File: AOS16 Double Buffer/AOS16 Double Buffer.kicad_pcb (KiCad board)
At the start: 4 copper layers, 100 x 100 mm, 18 parts, among them IC1 SN74AUP2G14DCKR, IC10 SN74LVC16245ADGVR, IC11 SN74LVC16245ADGVR, IC2 SN74LVC16245ADGVR, IC3 IS61WV3216BLL-12TLI, IC4 SN74LVC16245ADGVR, IC5 SN74LVC16245ADGVR, IC6 SN74LVC16245ADGVR, IC7 IS61WV3216BLL-12TLI, IC8 SN74LVC16245ADGVR, IC9 SN74LVC16245ADGVR, J1 Conn_01x07_Pin, J2 Conn_02x08_Top_Bottom, J3 Conn_02x08_Odd_Even, J4 Conn_02x08_Odd_Even, J5 Conn_02x08_Top_Bottom, U1 74LS157, U2 74LS157

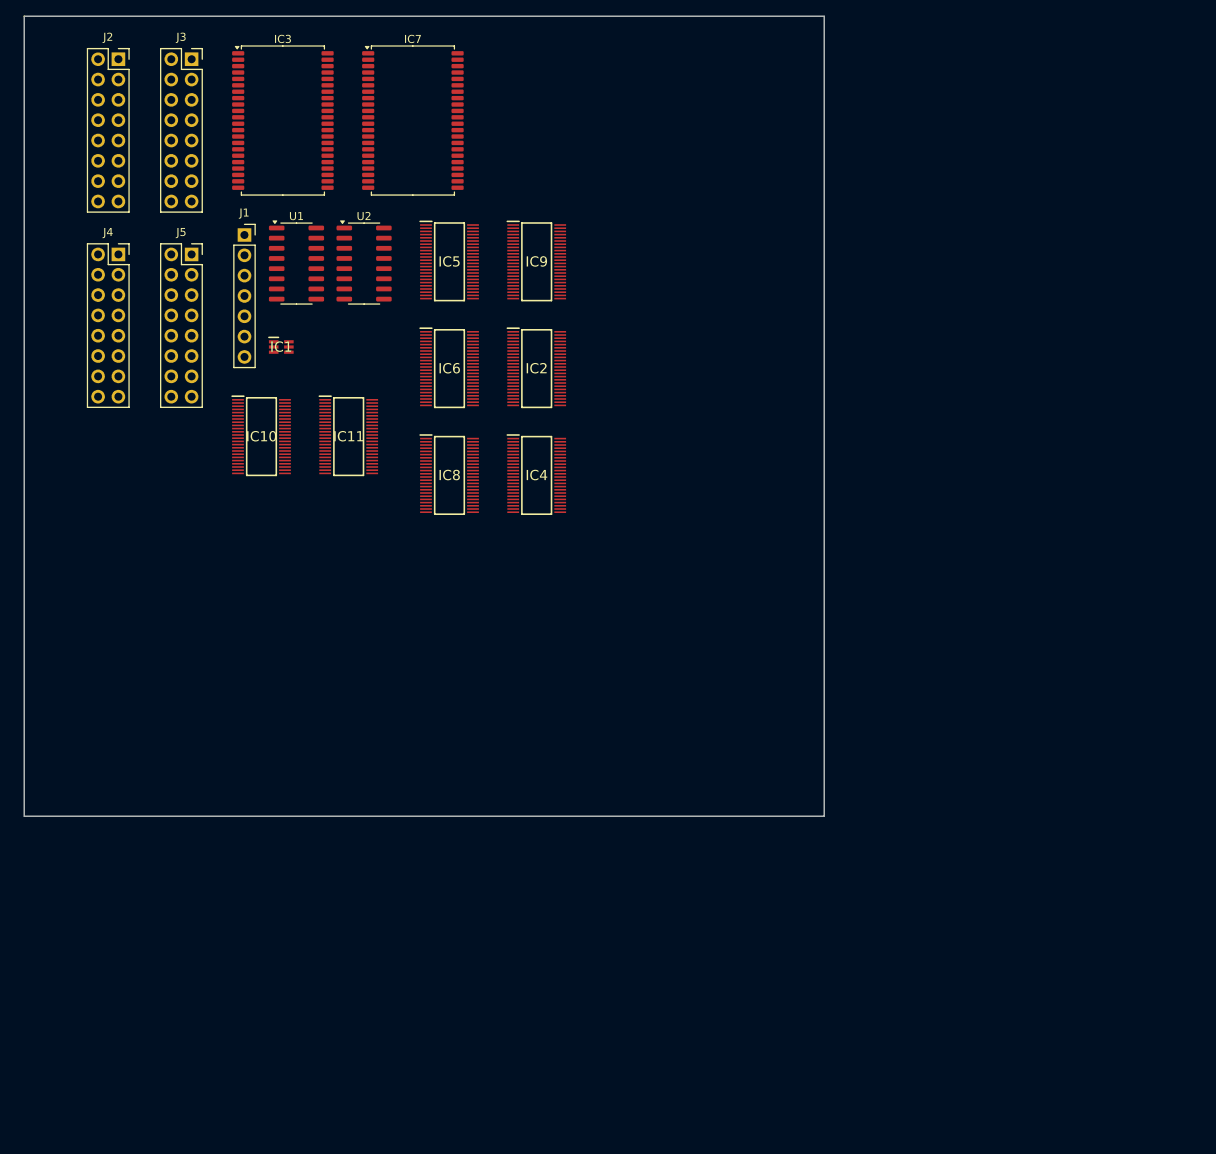
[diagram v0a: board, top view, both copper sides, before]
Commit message: updated double buffer
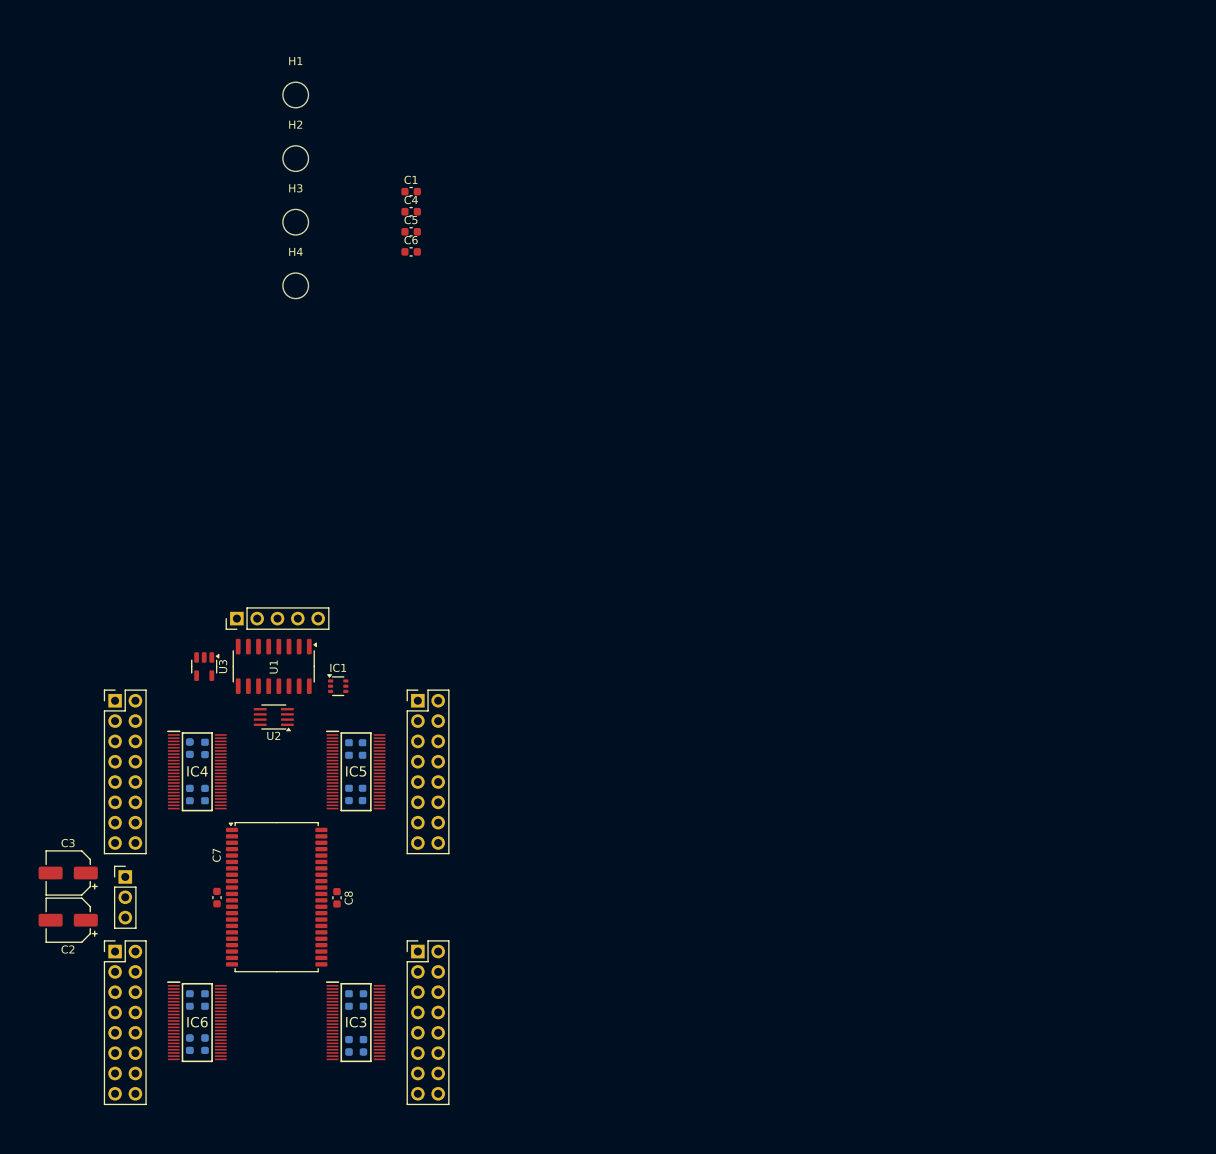
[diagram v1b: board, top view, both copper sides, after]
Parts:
- removed IC10, IC11, IC8, IC9: SN74LVC16245ADGVR, sn74lvc:SOP40P640X120-48N
- removed IC7: IS61WV3216BLL-12TLI, Package_SO:TSOP-II-44_10.16x18.41mm_P0.8mm
- added C1: 0.1uF, Capacitor_SMD:C_0603_1608Metric, F.Cu at (73.4, 46.9)
- added C10: 0.1uF, Capacitor_SMD:C_0603_1608Metric, B.Cu at (67.3, 116.6)
- added C11: 0.1uF, Capacitor_SMD:C_0603_1608Metric, B.Cu at (67.3, 122.3)
- added C12: 0.1uF, Capacitor_SMD:C_0603_1608Metric, B.Cu at (65.6, 122.3)
- added C13: 0.1uF, Capacitor_SMD:C_0603_1608Metric, B.Cu at (45.7, 116.5)
- added C14: 0.1uF, Capacitor_SMD:C_0603_1608Metric, B.Cu at (47.6, 116.5)
- added C15: 0.1uF, Capacitor_SMD:C_0603_1608Metric, B.Cu at (47.6, 122.3)
- added C16: 0.1uF, Capacitor_SMD:C_0603_1608Metric, B.Cu at (45.7, 122.3)
- added C17: 0.1uF, Capacitor_SMD:C_0603_1608Metric, B.Cu at (65.6, 148.0)
- added C18: 0.1uF, Capacitor_SMD:C_0603_1608Metric, B.Cu at (67.4, 148.0)
- added C19: 0.1uF, Capacitor_SMD:C_0603_1608Metric, B.Cu at (65.6, 153.7)
- added C2: 100 uF, Capacitor_SMD:CP_Elec_5x5.3, F.Cu at (30.5, 138.0)
- added C20: 0.1uF, Capacitor_SMD:C_0603_1608Metric, B.Cu at (67.4, 153.7)
- added C21: 0.1uF, Capacitor_SMD:C_0603_1608Metric, B.Cu at (45.7, 148.0)
- added C22: 0.1uF, Capacitor_SMD:C_0603_1608Metric, B.Cu at (47.6, 148.0)
- added C23: 0.1uF, Capacitor_SMD:C_0603_1608Metric, B.Cu at (47.6, 153.5)
- added C24: 0.1uF, Capacitor_SMD:C_0603_1608Metric, B.Cu at (45.7, 153.5)
- added C3: 100 uF, Capacitor_SMD:CP_Elec_5x5.3, F.Cu at (30.5, 132.1)
- added C4: 0.1uF, Capacitor_SMD:C_0603_1608Metric, F.Cu at (73.4, 49.4)
- added C5: 0.1uF, Capacitor_SMD:C_0603_1608Metric, F.Cu at (73.4, 52.0)
- added C6: 0.1uF, Capacitor_SMD:C_0603_1608Metric, F.Cu at (73.4, 54.5)
- added C7: 0.1uF, Capacitor_SMD:C_0603_1608Metric, F.Cu at (49.1, 135.2)
- added C8: 0.1uF, Capacitor_SMD:C_0603_1608Metric, F.Cu at (64.1, 135.2)
- added C9: 0.1uF, Capacitor_SMD:C_0603_1608Metric, B.Cu at (65.6, 116.6)
- added H1: M3, MountingHole:MountingHole_3.2mm_M3, F.Cu at (58.9, 34.9)
- added H2: M3, MountingHole:MountingHole_3.2mm_M3, F.Cu at (58.9, 42.8)
- added H3: M3, MountingHole:MountingHole_3.2mm_M3, F.Cu at (58.9, 50.8)
- added H4: M3, MountingHole:MountingHole_3.2mm_M3, F.Cu at (58.9, 58.7)
- added J6: Conn_02x08_Top_Bottom, Connector_PinHeader_2.54mm:PinHeader_2x08_P2.54mm_Vertical, F.Cu at (74.2, 110.6)
- added U3: 74AHC1G08, Package_TO_SOT_SMD:SOT-23-5, F.Cu at (47.5, 106.3)
- IC1: footprint sn74aup2:SOT65P210X110-6N -> Package_TO_SOT_SMD:SOT-363_SC-70-6
- IC2: value SN74LVC16245ADGVR -> IS61WV3216BLL-12TLI; footprint sn74lvc:SOP40P640X120-48N -> Package_SO:TSOP-II-44_10.16x18.41mm_P0.8mm
- IC3: value IS61WV3216BLL-12TLI -> SN74LVC16245ADGVR; footprint Package_SO:TSOP-II-44_10.16x18.41mm_P0.8mm -> sn74lvc:SOP40P640X120-48N
- J1: value Conn_01x07_Pin -> Conn_01x03_Pin; footprint Connector_PinSocket_2.54mm:PinSocket_1x07_P2.54mm_Vertical -> Connector_PinHeader_2.54mm:PinHeader_1x03_P2.54mm_Vertical
- J2: value Conn_02x08_Top_Bottom -> Conn_01x05_Pin; footprint Connector_PinSocket_2.54mm:PinSocket_2x08_P2.54mm_Vertical -> Connector_PinHeader_2.54mm:PinHeader_1x05_P2.54mm_Vertical
- J3, J4: value Conn_02x08_Odd_Even -> Conn_02x08_Top_Bottom; footprint Connector_PinSocket_2.54mm:PinSocket_2x08_P2.54mm_Vertical -> Connector_PinHeader_2.54mm:PinHeader_2x08_P2.54mm_Vertical
- J5: footprint Connector_PinSocket_2.54mm:PinSocket_2x08_P2.54mm_Vertical -> Connector_PinHeader_2.54mm:PinHeader_2x08_P2.54mm_Vertical
- U2: value 74LS157 -> 74AUC2G32; footprint Package_SO:SOIC-16_3.9x9.9mm_P1.27mm -> Package_SO:SSOP-8_2.95x2.8mm_P0.65mm
- moved IC3 113.1 mm to (66.5, 150.8)
- moved J3 111.9 mm to (36.4, 141.9)
- moved J4 94.8 mm to (74.2, 141.9)
- moved IC6 87.6 mm to (46.6, 150.8)
- moved J1 81.6 mm to (37.6, 132.6)
- moved IC2 73.6 mm to (56.6, 135.1)
- moved J2 71.5 mm to (51.6, 100.3), turned to 90 degrees
- moved IC5 64.8 mm to (66.5, 119.4)
- moved U2 57.8 mm to (56.2, 112.6), turned to 180 degrees
- moved J5 56.6 mm to (36.4, 110.6)
- moved IC4 56.3 mm to (46.6, 119.4)
- moved U1 50.4 mm to (56.2, 106.3), turned to -90 degrees
- moved IC1 43.0 mm to (64.2, 108.8)
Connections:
- IC1 pad 1: /GSEL -> /SEL
- IC1 pad 3: unconnected-(IC1-2A-Pad3) -> /W1
- IC1 pad 4: unconnected-(IC1-2Y-Pad4) -> /~{W1}
- IC1 pad 6: /~{GSEL} -> /~{SEL}
- IC2 pad 1: VCC -> unconnected-(IC2-NC_1-Pad1)
- IC2 pad 10: GND -> /ram/OUT9
- IC2 pad 11: /word_conn/IN6 -> +3.3V
- IC2 pad 12: /word_conn/IN7 -> GND
- IC2 pad 13: /word_conn/IN8 -> /ram/OUT7
- IC2 pad 14: /word_conn/IN9 -> /ram/OUT5
- IC2 pad 15: GND -> /ram/OUT3
- IC2 pad 16: /word_conn/IN10 -> /ram/OUT1
- IC2 pad 17: /word_conn/IN11 -> /W
- IC2 pad 18: VCC -> /ram/INA8
- IC2 pad 19: /word_conn/IN12 -> /ram/INA10
- IC2 pad 2: /word_conn/IN0 -> /ram/INA1
- IC2 pad 20: /word_conn/IN13 -> /ram/INA12
- IC2 pad 21: GND -> /ram/INA14
- IC2 pad 22: /word_conn/IN14 -> unconnected-(IC2-NC_2-Pad22)
- IC2 pad 23: /word_conn/IN15 -> unconnected-(IC2-NC_3-Pad23)
- IC2 pad 24: VCC -> /ram/INA13
- IC2 pad 25: /GSEL -> /ram/INA11
- IC2 pad 26: /word_buffer/A15 -> /ram/INA9
- IC2 pad 27: /word_buffer/A14 -> /ram/INA7
- IC2 pad 28: GND -> unconnected-(IC2-NC_4-Pad28)
- IC2 pad 29: /word_buffer/A13 -> /ram/OUT0
- IC2 pad 3: /word_conn/IN1 -> /ram/INA3
- IC2 pad 30: /word_buffer/A12 -> /ram/OUT2
- IC2 pad 31: VCC -> /ram/OUT4
- IC2 pad 32: /word_buffer/A11 -> /ram/OUT6
- IC2 pad 33: /word_buffer/A10 -> +3.3V
- IC2 pad 35: /word_buffer/A9 -> /ram/OUT8
- IC2 pad 36: /word_buffer/A8 -> /ram/OUT14
- IC2 pad 37: /word_buffer/A7 -> /ram/OUT12
- IC2 pad 38: /word_buffer/A6 -> /ram/OUT10
- IC2 pad 4: GND -> /ram/INA5
- IC2 pad 40: /word_buffer/A5 -> GND
- IC2 pad 41: /word_buffer/A4 -> /R
- IC2 pad 42: VCC -> /ram/INA4
- IC2 pad 43: /word_buffer/A3 -> /ram/INA2
- IC2 pad 44: /word_buffer/A2 -> /ram/INA0
- IC2 pad 5: /word_conn/IN2 -> /ram/INA6
- IC2 pad 6: /word_conn/IN3 -> GND
- IC2 pad 7: VCC -> /ram/OUT11
- IC2 pad 8: /word_conn/IN4 -> /ram/OUT13
- IC2 pad 9: /word_conn/IN5 -> /ram/OUT15
- IC3 pad 1: unconnected-(IC3-NC_1-Pad1) -> VCC
- IC3 pad 10: /ram/OUT3 -> GND
- IC3 pad 11: VCC -> /ram/INA6
- IC3 pad 12: GND -> /ram/INA7
- IC3 pad 13: /ram/OUT4 -> /ram/INA8
- IC3 pad 14: /ram/OUT5 -> /ram/INA9
- IC3 pad 15: /ram/OUT6 -> GND
- IC3 pad 16: /ram/OUT7 -> /ram/INA10
- IC3 pad 17: /W1 -> /ram/INA11
- IC3 pad 18: /ram/INA10 -> VCC
- IC3 pad 19: /ram/INA9 -> /ram/INA12
- IC3 pad 2: /ram/INA14 -> /ram/INA0
- IC3 pad 20: /ram/INA8 -> /ram/INA13
- IC3 pad 21: /ram/INA7 -> GND
- IC3 pad 22: unconnected-(IC3-NC_2-Pad22) -> /ram/INA14
- IC3 pad 23: unconnected-(IC3-NC_3-Pad23) -> /word_buffer1/B15
- IC3 pad 24: /ram/INA6 -> VCC
- IC3 pad 25: /ram/INA5 -> /~{SEL}
- IC3 pad 26: /ram/INA4 -> /word_conn1/IN15
- IC3 pad 27: /ram/INA3 -> /word_conn1/IN14
- IC3 pad 28: unconnected-(IC3-NC_4-Pad28) -> GND
- IC3 pad 29: /ram/OUT8 -> /word_conn1/IN13
- IC3 pad 3: /ram/INA13 -> /ram/INA1
- IC3 pad 30: /ram/OUT9 -> /word_conn1/IN12
- IC3 pad 31: /ram/OUT10 -> VCC
- IC3 pad 32: /ram/OUT11 -> /word_conn1/IN11
- IC3 pad 33: VCC -> /word_conn1/IN10
- IC3 pad 35: /ram/OUT12 -> /word_conn1/IN9
- IC3 pad 36: /ram/OUT13 -> /word_conn1/IN8
- IC3 pad 37: /ram/OUT14 -> /word_conn1/IN7
- IC3 pad 38: /ram/OUT15 -> /word_conn1/IN6
- IC3 pad 4: /ram/INA12 -> GND
- IC3 pad 40: GND -> /word_conn1/IN5
- IC3 pad 41: /R1 -> /word_conn1/IN4
- IC3 pad 42: /ram/INA2 -> VCC
- IC3 pad 43: /ram/INA1 -> /word_conn1/IN3
- IC3 pad 44: /ram/INA0 -> /word_conn1/IN2
- IC3 pad 5: /ram/INA11 -> /ram/INA2
- IC3 pad 6: GND -> /ram/INA3
- IC3 pad 7: /ram/OUT0 -> VCC
- IC3 pad 8: /ram/OUT1 -> /ram/INA4
- IC3 pad 9: /ram/OUT2 -> /ram/INA5
- IC4 pad 1: VCC -> /W0
- IC4 pad 11: /word_buffer/A6 -> /word_conn2/IN6
- IC4 pad 12: /word_buffer/A7 -> /word_conn2/IN7
- IC4 pad 13: /word_buffer/A8 -> /word_conn2/IN8
- IC4 pad 14: /word_buffer/A9 -> /word_conn2/IN9
- IC4 pad 16: /word_buffer/A10 -> /word_conn2/IN10
- IC4 pad 17: /word_buffer/A11 -> /word_conn2/IN11
- IC4 pad 19: /word_buffer/A12 -> /word_conn2/IN12
- IC4 pad 2: /word_buffer/A0 -> /word_conn2/IN0
- IC4 pad 20: /word_buffer/A13 -> /word_conn2/IN13
- IC4 pad 22: /word_buffer/A14 -> /word_conn2/IN14
- IC4 pad 23: /word_buffer/A15 -> /word_conn2/IN15
- IC4 pad 24: VCC -> /W0
- IC4 pad 25: /~{GSEL} -> /E0
- IC4 pad 26: /word_conn1/IN15 -> /ram/OUT15
- IC4 pad 27: /word_conn1/IN14 -> /ram/OUT14
- IC4 pad 29: /word_conn1/IN13 -> /ram/OUT13
- IC4 pad 3: /word_buffer/A1 -> /word_conn2/IN1
- IC4 pad 30: /word_conn1/IN12 -> /ram/OUT12
- IC4 pad 32: /word_conn1/IN11 -> /ram/OUT11
- IC4 pad 33: /word_conn1/IN10 -> /ram/OUT10
- IC4 pad 35: /word_conn1/IN9 -> /ram/OUT9
- IC4 pad 36: /word_conn1/IN8 -> /ram/OUT8
- IC4 pad 37: /word_conn1/IN7 -> /ram/OUT7
- IC4 pad 38: /word_conn1/IN6 -> /ram/OUT6
- IC4 pad 40: /word_conn1/IN5 -> /ram/OUT5
- IC4 pad 41: /word_conn1/IN4 -> /ram/OUT4
- IC4 pad 43: /word_conn1/IN3 -> /ram/OUT3
- IC4 pad 44: /word_conn1/IN2 -> /ram/OUT2
- IC4 pad 46: /word_conn1/IN1 -> /ram/OUT1
- IC4 pad 47: /word_conn1/IN0 -> /ram/OUT0
- IC4 pad 48: /~{GSEL} -> /E0
- IC4 pad 5: /word_buffer/A2 -> /word_conn2/IN2
- IC4 pad 6: /word_buffer/A3 -> /word_conn2/IN3
- IC4 pad 8: /word_buffer/A4 -> /word_conn2/IN4
- IC4 pad 9: /word_buffer/A5 -> /word_conn2/IN5
- IC5 pad 1: GND -> /~{W1}
- IC5 pad 11: /word_conn/IN6 -> /ram/OUT6
- IC5 pad 12: /word_conn/IN7 -> /ram/OUT7
- IC5 pad 13: /word_conn/IN8 -> /ram/OUT8
- IC5 pad 14: /word_conn/IN9 -> /ram/OUT9
- IC5 pad 16: /word_conn/IN10 -> /ram/OUT10
- IC5 pad 17: /word_conn/IN11 -> /ram/OUT11
- IC5 pad 19: /word_conn/IN12 -> /ram/OUT12
- IC5 pad 2: /word_conn/IN0 -> /ram/OUT0
- IC5 pad 20: /word_conn/IN13 -> /ram/OUT13
- IC5 pad 22: /word_conn/IN14 -> /ram/OUT14
- IC5 pad 23: /word_conn/IN15 -> /ram/OUT15
- IC5 pad 24: GND -> /~{W1}
- IC5 pad 25: /~{GSEL} -> /E1
- IC5 pad 26: /word_buffer2/A15 -> /word_conn3/IN15
- IC5 pad 27: /word_buffer2/A14 -> /word_conn3/IN14
- IC5 pad 29: /word_buffer2/A13 -> /word_conn3/IN13
- IC5 pad 3: /word_conn/IN1 -> /ram/OUT1
- IC5 pad 30: /word_buffer2/A12 -> /word_conn3/IN12
- IC5 pad 32: /word_buffer2/A11 -> /word_conn3/IN11
- IC5 pad 33: /word_buffer2/A10 -> /word_conn3/IN10
- IC5 pad 35: /word_buffer2/A9 -> /word_conn3/IN9
- IC5 pad 36: /word_buffer2/A8 -> /word_conn3/IN8
- IC5 pad 37: /word_buffer2/A7 -> /word_conn3/IN7
- IC5 pad 38: /word_buffer2/A6 -> /word_conn3/IN6
- IC5 pad 40: /word_buffer2/A5 -> /word_conn3/IN5
- IC5 pad 41: /word_buffer2/A4 -> /word_conn3/IN4
- IC5 pad 43: /word_buffer2/A3 -> /word_conn3/IN3
- IC5 pad 44: /word_buffer2/A2 -> /word_conn3/IN2
- IC5 pad 46: /word_buffer2/A1 -> /word_conn3/IN1
- IC5 pad 47: /word_buffer2/A0 -> /word_conn3/IN0
- IC5 pad 48: /~{GSEL} -> /E1
- IC5 pad 5: /word_conn/IN2 -> /ram/OUT2
- IC5 pad 6: /word_conn/IN3 -> /ram/OUT3
- IC5 pad 8: /word_conn/IN4 -> /ram/OUT4
- IC5 pad 9: /word_conn/IN5 -> /ram/OUT5
- IC6 pad 11: /word_conn1/IN6 -> /word_conn/IN6
- IC6 pad 12: /word_conn1/IN7 -> /word_conn/IN7
- IC6 pad 13: /word_conn1/IN8 -> /word_conn/IN8
- IC6 pad 14: /word_conn1/IN9 -> /word_conn/IN9
- IC6 pad 16: /word_conn1/IN10 -> /word_conn/IN10
- IC6 pad 17: /word_conn1/IN11 -> /word_conn/IN11
- IC6 pad 19: /word_conn1/IN12 -> /word_conn/IN12
- IC6 pad 2: /word_conn1/IN0 -> /word_conn/IN0
- IC6 pad 20: /word_conn1/IN13 -> /word_conn/IN13
- IC6 pad 22: /word_conn1/IN14 -> /word_conn/IN14
- IC6 pad 23: /word_conn1/IN15 -> /word_conn/IN15
- IC6 pad 25: /GSEL -> /SEL
- IC6 pad 26: /word_buffer2/A15 -> /word_buffer/A15
- IC6 pad 27: /word_buffer2/A14 -> /ram/INA14
- IC6 pad 29: /word_buffer2/A13 -> /ram/INA13
- IC6 pad 3: /word_conn1/IN1 -> /word_conn/IN1
- IC6 pad 30: /word_buffer2/A12 -> /ram/INA12
- IC6 pad 32: /word_buffer2/A11 -> /ram/INA11
- IC6 pad 33: /word_buffer2/A10 -> /ram/INA10
- IC6 pad 35: /word_buffer2/A9 -> /ram/INA9
- IC6 pad 36: /word_buffer2/A8 -> /ram/INA8
- IC6 pad 37: /word_buffer2/A7 -> /ram/INA7
- IC6 pad 38: /word_buffer2/A6 -> /ram/INA6
- IC6 pad 40: /word_buffer2/A5 -> /ram/INA5
- IC6 pad 41: /word_buffer2/A4 -> /ram/INA4
- IC6 pad 43: /word_buffer2/A3 -> /ram/INA3
- IC6 pad 44: /word_buffer2/A2 -> /ram/INA2
- IC6 pad 46: /word_buffer2/A1 -> /ram/INA1
- IC6 pad 47: /word_buffer2/A0 -> /ram/INA0
- IC6 pad 48: /GSEL -> /SEL
- IC6 pad 5: /word_conn1/IN2 -> /word_conn/IN2
- IC6 pad 6: /word_conn1/IN3 -> /word_conn/IN3
- IC6 pad 8: /word_conn1/IN4 -> /word_conn/IN4
- IC6 pad 9: /word_conn1/IN5 -> /word_conn/IN5
- J1 pad 1: VCC -> +3.3V
- J1 pad 2: GND -> VCC
- J1 pad 3: /CW -> GND
- J2 pad 1: /word_conn/IN0 -> /W1
- J2 pad 2: /word_conn/IN1 -> /W0
- J2 pad 3: /word_conn/IN2 -> /R1
- J2 pad 4: /word_conn/IN3 -> /R0
- J2 pad 5: /word_conn/IN4 -> /SEL
- J3 pad 1: /word_conn_flip1/IN1 -> /word_conn/IN0
- J3 pad 10: /word_conn_flip1/IN8 -> /word_conn/IN9
- J3 pad 11: /word_conn_flip1/IN11 -> /word_conn/IN10
- J3 pad 12: /word_conn_flip1/IN10 -> /word_conn/IN11
- J3 pad 13: /word_conn_flip1/IN13 -> /word_conn/IN12
- J3 pad 14: /word_conn_flip1/IN12 -> /word_conn/IN13
- J3 pad 15: /word_conn_flip1/IN15 -> /word_conn/IN14
- J3 pad 16: /word_conn_flip1/IN14 -> /word_conn/IN15
- J3 pad 2: /word_conn_flip1/IN0 -> /word_conn/IN1
- J3 pad 3: /word_conn_flip1/IN3 -> /word_conn/IN2
- J3 pad 4: /word_conn_flip1/IN2 -> /word_conn/IN3
- J3 pad 5: /word_conn_flip1/IN5 -> /word_conn/IN4
- J3 pad 6: /word_conn_flip1/IN4 -> /word_conn/IN5
- J3 pad 7: /word_conn_flip1/IN7 -> /word_conn/IN6
- J3 pad 8: /word_conn_flip1/IN6 -> /word_conn/IN7
- J3 pad 9: /word_conn_flip1/IN9 -> /word_conn/IN8
- J4 pad 1: /word_conn_flip2/IN1 -> /word_conn1/IN0
- J4 pad 10: /word_conn_flip2/IN8 -> /word_conn1/IN9
- J4 pad 11: /word_conn_flip2/IN11 -> /word_conn1/IN10
- J4 pad 12: /word_conn_flip2/IN10 -> /word_conn1/IN11
- J4 pad 13: /word_conn_flip2/IN13 -> /word_conn1/IN12
- J4 pad 14: /word_conn_flip2/IN12 -> /word_conn1/IN13
- J4 pad 15: /word_conn_flip2/IN15 -> /word_conn1/IN14
- J4 pad 16: /word_conn_flip2/IN14 -> /word_conn1/IN15
- J4 pad 2: /word_conn_flip2/IN0 -> /word_conn1/IN1
- J4 pad 3: /word_conn_flip2/IN3 -> /word_conn1/IN2
- J4 pad 4: /word_conn_flip2/IN2 -> /word_conn1/IN3
- J4 pad 5: /word_conn_flip2/IN5 -> /word_conn1/IN4
- J4 pad 6: /word_conn_flip2/IN4 -> /word_conn1/IN5
- J4 pad 7: /word_conn_flip2/IN7 -> /word_conn1/IN6
- J4 pad 8: /word_conn_flip2/IN6 -> /word_conn1/IN7
- J4 pad 9: /word_conn_flip2/IN9 -> /word_conn1/IN8
- J5 pad 1: /word_conn1/IN0 -> /word_conn2/IN0
- J5 pad 10: /word_conn1/IN9 -> /word_conn2/IN9
- J5 pad 11: /word_conn1/IN10 -> /word_conn2/IN10
- J5 pad 12: /word_conn1/IN11 -> /word_conn2/IN11
- J5 pad 13: /word_conn1/IN12 -> /word_conn2/IN12
- J5 pad 14: /word_conn1/IN13 -> /word_conn2/IN13
- J5 pad 15: /word_conn1/IN14 -> /word_conn2/IN14
- J5 pad 16: /word_conn1/IN15 -> /word_conn2/IN15
- J5 pad 2: /word_conn1/IN1 -> /word_conn2/IN1
- J5 pad 3: /word_conn1/IN2 -> /word_conn2/IN2
- J5 pad 4: /word_conn1/IN3 -> /word_conn2/IN3
- J5 pad 5: /word_conn1/IN4 -> /word_conn2/IN4
- J5 pad 6: /word_conn1/IN5 -> /word_conn2/IN5
- J5 pad 7: /word_conn1/IN6 -> /word_conn2/IN6
- J5 pad 8: /word_conn1/IN7 -> /word_conn2/IN7
- J5 pad 9: /word_conn1/IN8 -> /word_conn2/IN8
- U1 pad 1: /GSEL -> /SEL
- U1 pad 2: /GR -> /R0
- U1 pad 3: /CR -> /R1
- U1 pad 4: /R1 -> /R
- U1 pad 5: /GW -> /W0
- U1 pad 6: /CW -> /W1
- U1 pad 7: /W1 -> /W
- U2 pad 1: /~{GSEL} -> Net-(U2-Pad1)
- U2 pad 2: /GR -> /~{SEL}
- U2 pad 3: /CR -> /E1
- U2 pad 4: /R2 -> GND
- U2 pad 5: /GW -> /SEL
- U2 pad 6: /CW -> Net-(U2-Pad1)
- U2 pad 7: /W2 -> /E0
- U2 pad 8: GND -> VCC
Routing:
- removed copper zone on In1.Cu, net GND
- removed copper zone on In2.Cu, net VCC
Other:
- board outline removed

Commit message: Added Logisim schematic
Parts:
- moved C3 44.7 mm to (75.1, 135.1), turned to -90 degrees
- moved C2 3.45 mm to (32.4, 135.1), turned to -90 degrees
- moved C19 0.12 mm to (65.6, 153.6)
- moved C20 0.12 mm to (67.4, 153.6)
- moved C23 0.07 mm to (47.6, 153.6)
- moved C24 0.07 mm to (45.7, 153.6)
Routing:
- net /ram/INA2: track 0.00 -> 35.8 mm, vias 0 -> 2
- net /ram/INA3: track 0.00 -> 35.6 mm, vias 0 -> 1
- net /ram/INA0: track 0.00 -> 34.8 mm, vias 0 -> 2
- net /ram/INA1: track 0.00 -> 34.5 mm, vias 0 -> 2
- net /ram/INA9: track 0.00 -> 14.2 mm
- net /ram/INA6: track 0.00 -> 14.2 mm
- net /ram/INA13: track 0.00 -> 14.1 mm
- net /ram/INA11: track 0.00 -> 14.1 mm
- net /ram/INA4: track 0.00 -> 14.1 mm
- net /ram/INA8: track 0.00 -> 14.1 mm
- net /ram/INA7: track 0.00 -> 14.1 mm
- net /ram/INA5: track 0.00 -> 14.0 mm
- net /ram/INA14: track 0.00 -> 14.0 mm
- net /ram/INA12: track 0.00 -> 14.0 mm
- net /ram/INA10: track 0.00 -> 14.0 mm
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- added copper zone on B.Cu, net GND
- added copper zone on In1.Cu, net GND
- added copper zone on F.Cu, net VCC
- added copper zone on In2.Cu, net VCC

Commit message: Completed double buffer first draft
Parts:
- removed H1, H2, H3, H4: M3, MountingHole:MountingHole_3.2mm_M3
- removed IC6: SN74LVC16245ADGVR, sn74lvc:SOP40P640X120-48N
- added C25: 0.01uF, Capacitor_SMD:C_0603_1608Metric, B.Cu at (39.1, 106.5)
- added C26: 0.01uF, Capacitor_SMD:C_0603_1608Metric, B.Cu at (36.0, 113.5)
- added C27: 0.01uF, Capacitor_SMD:C_0603_1608Metric, B.Cu at (39.1, 113.5)
- added U4: 74AHC1G32, Package_TO_SOT_SMD:SOT-353_SC-70-5, F.Cu at (61.7, 68.3)
- added U5: 74AHC1G04, Package_TO_SOT_SMD:SOT-353_SC-70-5, F.Cu at (58.3, 64.7)
- added U6: 74AHC1G04, Package_TO_SOT_SMD:SOT-353_SC-70-5, F.Cu at (54.2, 68.3)
- added U7: 74LS157, Package_SO:SOIC-16_3.9x9.9mm_P1.27mm, F.Cu at (41.5, 58.5)
- C10, C11, C9: moved to F.Cu
- C12, C13, C14, C15, C16, C17, C18, C19, C20, C21, C22, C23, C24: value 0.1uF -> 0.01uF
- C2: value 100 uF -> 0.1uF; footprint Capacitor_SMD:CP_Elec_5x5.3 -> Capacitor_SMD:C_0603_1608Metric
- C4: value 0.1uF -> 100 uF; footprint Capacitor_SMD:C_0603_1608Metric -> Capacitor_SMD:CP_Elec_5x5.3
- IC1: value SN74AUP2G14DCKR -> IS61WV3216BLL-12TLI; footprint Package_TO_SOT_SMD:SOT-363_SC-70-6 -> Package_SO:TSOP-II-44_10.16x18.41mm_P0.8mm
- IC2: value IS61WV3216BLL-12TLI -> SN74LVC16245ADGVR; footprint Package_SO:TSOP-II-44_10.16x18.41mm_P0.8mm -> Package_SO:TSSOP-48_6.1x12.5mm_P0.5mm
- IC3, IC4, IC5: footprint sn74lvc:SOP40P640X120-48N -> Package_SO:TSSOP-48_6.1x12.5mm_P0.5mm
- J1: value Conn_01x03_Pin -> Conn_01x02_Pin; footprint Connector_PinHeader_2.54mm:PinHeader_1x03_P2.54mm_Vertical -> Connector_PinHeader_2.54mm:PinHeader_1x02_P2.54mm_Vertical
- J2: value Conn_01x05_Pin -> Conn_02x08_Top_Bottom; footprint Connector_PinHeader_2.54mm:PinHeader_1x05_P2.54mm_Vertical -> Connector_PinHeader_2.54mm:PinHeader_2x08_P2.54mm_Vertical
- J6: value Conn_02x08_Top_Bottom -> Conn_01x07_Pin; footprint Connector_PinHeader_2.54mm:PinHeader_2x08_P2.54mm_Vertical -> Connector_PinHeader_2.54mm:PinHeader_1x07_P2.54mm_Vertical
- U1: value 74LS157 -> 74AHC1G08; footprint Package_SO:SOIC-16_3.9x9.9mm_P1.27mm -> Package_TO_SOT_SMD:SOT-353_SC-70-5
- U2: value 74AUC2G32 -> 74AHC1G08; footprint Package_SO:SSOP-8_2.95x2.8mm_P0.65mm -> Package_TO_SOT_SMD:SOT-353_SC-70-5
- U3: value 74AHC1G08 -> 74AHC1G32; footprint Package_TO_SOT_SMD:SOT-23-5 -> Package_TO_SOT_SMD:SOT-353_SC-70-5
- moved J4 88.1 mm to (26.5, 67.9)
- moved C20 81.1 mm to (55.7, 73.3), turned to 90 degrees
- moved IC3 79.5 mm to (37.5, 76.8)
- moved C17 79.3 mm to (39.1, 73.3)
- moved C19 78.0 mm to (39.1, 80.2)
- moved C21 75.8 mm to (58.9, 73.3)
- moved C18 74.7 mm to (36.0, 80.2), turned to -90 degrees
- moved C23 74.2 mm to (58.9, 80.2)
- moved C7 71.2 mm to (56.0, 64.3), turned to 90 degrees
- moved C2 71.2 mm to (45.6, 65.2), turned to 90 degrees
- moved C22 68.2 mm to (55.7, 80.2), turned to -90 degrees
- moved J6 67.9 mm to (39.8, 52.0), turned to 90 degrees
- moved C8 67.0 mm to (56.6, 68.6)
- moved C9 65.4 mm to (35.4, 58.6)
- moved C3 59.9 mm to (32.0, 93.5)
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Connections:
- C10 pad 1: VCC -> +3.3V
- C11 pad 1: VCC -> +3.3V
- C12 pad 1: VCC -> +3.3V
- C13 pad 1: VCC -> +3.3V
- C14 pad 1: VCC -> +3.3V
- C15 pad 1: VCC -> +3.3V
- C16 pad 1: VCC -> +3.3V
- C17 pad 1: VCC -> +3.3V
- C18 pad 1: VCC -> +3.3V
- C19 pad 1: VCC -> +3.3V
- C2 pad 1: +3.3V -> VCC
- C20 pad 1: VCC -> +3.3V
- C21 pad 1: VCC -> +3.3V
- C22 pad 1: VCC -> +3.3V
- C23 pad 1: VCC -> +3.3V
- C24 pad 1: VCC -> +3.3V
- C3 pad 1: VCC -> +3.3V
- C4 pad 1: GND -> VCC
- C4 pad 2: VCC -> GND
- C5 pad 1: GND -> VCC
- C5 pad 2: VCC -> GND
- C7 pad 1: +3.3V -> VCC
- C8 pad 1: +3.3V -> VCC
- IC1 pad 1: /SEL -> unconnected-(IC1-NC_1-Pad1)
- IC1 pad 2: GND -> /ram/INA1
- IC1 pad 3: /W1 -> /ram/INA3
- IC1 pad 4: /~{W1} -> /ram/INA5
- IC1 pad 5: VCC -> /ram/INA6
- IC1 pad 6: /~{SEL} -> GND
- IC2 pad 1: unconnected-(IC2-NC_1-Pad1) -> +3.3V
- IC2 pad 10: /ram/OUT9 -> GND
- IC2 pad 11: +3.3V -> /ram/INA6
- IC2 pad 12: GND -> /ram/INA7
- IC2 pad 13: /ram/OUT7 -> /ram/INA8
- IC2 pad 14: /ram/OUT5 -> /ram/INA9
- IC2 pad 15: /ram/OUT3 -> GND
- IC2 pad 16: /ram/OUT1 -> /ram/INA10
- IC2 pad 17: /W -> /ram/INA11
- IC2 pad 18: /ram/INA8 -> +3.3V
- IC2 pad 19: /ram/INA10 -> /ram/INA12
- IC2 pad 2: /ram/INA1 -> /ram/INA0
- IC2 pad 20: /ram/INA12 -> /ram/INA13
- IC2 pad 21: /ram/INA14 -> GND
- IC2 pad 22: unconnected-(IC2-NC_2-Pad22) -> /ram/INA14
- IC2 pad 23: unconnected-(IC2-NC_3-Pad23) -> /word_buffer1/B15
- IC2 pad 24: /ram/INA13 -> +3.3V
- IC2 pad 25: /ram/INA11 -> /~{SEL}
- IC2 pad 26: /ram/INA9 -> /word_conn1/IN15
- IC2 pad 27: /ram/INA7 -> /word_conn1/IN14
- IC2 pad 28: unconnected-(IC2-NC_4-Pad28) -> GND
- IC2 pad 29: /ram/OUT0 -> /word_conn1/IN13
- IC2 pad 3: /ram/INA3 -> /ram/INA1
- IC2 pad 30: /ram/OUT2 -> /word_conn1/IN12
- IC2 pad 31: /ram/OUT4 -> +3.3V
- IC2 pad 32: /ram/OUT6 -> /word_conn1/IN11
- IC2 pad 33: +3.3V -> /word_conn1/IN10
- IC2 pad 35: /ram/OUT8 -> /word_conn1/IN9
- IC2 pad 36: /ram/OUT14 -> /word_conn1/IN8
- IC2 pad 37: /ram/OUT12 -> /word_conn1/IN7
- IC2 pad 38: /ram/OUT10 -> /word_conn1/IN6
- IC2 pad 4: /ram/INA5 -> GND
- IC2 pad 40: GND -> /word_conn1/IN5
- IC2 pad 41: /R -> /word_conn1/IN4
- IC2 pad 42: /ram/INA4 -> +3.3V
- IC2 pad 43: /ram/INA2 -> /word_conn1/IN3
- IC2 pad 44: /ram/INA0 -> /word_conn1/IN2
- IC2 pad 5: /ram/INA6 -> /ram/INA2
- IC2 pad 6: GND -> /ram/INA3
- IC2 pad 7: /ram/OUT11 -> +3.3V
- IC2 pad 8: /ram/OUT13 -> /ram/INA4
- IC2 pad 9: /ram/OUT15 -> /ram/INA5
- IC3 pad 1: VCC -> /W0
- IC3 pad 11: /ram/INA6 -> /word_conn2/IN6
- IC3 pad 12: /ram/INA7 -> /word_conn2/IN7
- IC3 pad 13: /ram/INA8 -> /word_conn2/IN8
- IC3 pad 14: /ram/INA9 -> /word_conn2/IN9
- IC3 pad 16: /ram/INA10 -> /word_conn2/IN10
- IC3 pad 17: /ram/INA11 -> /word_conn2/IN11
- IC3 pad 18: VCC -> +3.3V
- IC3 pad 19: /ram/INA12 -> /word_conn2/IN12
- IC3 pad 2: /ram/INA0 -> /word_conn2/IN0
- IC3 pad 20: /ram/INA13 -> /word_conn2/IN13
- IC3 pad 22: /ram/INA14 -> /word_conn2/IN14
- IC3 pad 23: /word_buffer1/B15 -> /word_conn2/IN15
- IC3 pad 24: VCC -> /W0
- IC3 pad 25: /~{SEL} -> /E0
- IC3 pad 26: /word_conn1/IN15 -> /ram/OUT15
- IC3 pad 27: /word_conn1/IN14 -> /ram/OUT14
- IC3 pad 29: /word_conn1/IN13 -> /ram/OUT13
- IC3 pad 3: /ram/INA1 -> /word_conn2/IN1
- IC3 pad 30: /word_conn1/IN12 -> /ram/OUT12
- IC3 pad 31: VCC -> +3.3V
- IC3 pad 32: /word_conn1/IN11 -> /ram/OUT11
- IC3 pad 33: /word_conn1/IN10 -> /ram/OUT10
- IC3 pad 35: /word_conn1/IN9 -> /ram/OUT9
- IC3 pad 36: /word_conn1/IN8 -> /ram/OUT8
- IC3 pad 37: /word_conn1/IN7 -> /ram/OUT7
- IC3 pad 38: /word_conn1/IN6 -> /ram/OUT6
- IC3 pad 40: /word_conn1/IN5 -> /ram/OUT5
- IC3 pad 41: /word_conn1/IN4 -> /ram/OUT4
- IC3 pad 42: VCC -> +3.3V
- IC3 pad 43: /word_conn1/IN3 -> /ram/OUT3
- IC3 pad 44: /word_conn1/IN2 -> /ram/OUT2
- IC3 pad 46: /word_conn1/IN1 -> /ram/OUT1
- IC3 pad 47: /word_conn1/IN0 -> /ram/OUT0
- IC3 pad 48: /~{SEL} -> /E0
- IC3 pad 5: /ram/INA2 -> /word_conn2/IN2
- IC3 pad 6: /ram/INA3 -> /word_conn2/IN3
- IC3 pad 7: VCC -> +3.3V
- IC3 pad 8: /ram/INA4 -> /word_conn2/IN4
- IC3 pad 9: /ram/INA5 -> /word_conn2/IN5
- IC4 pad 1: /W0 -> /~{W1}
- IC4 pad 11: /word_conn2/IN6 -> /ram/OUT6
- IC4 pad 12: /word_conn2/IN7 -> /ram/OUT7
- IC4 pad 13: /word_conn2/IN8 -> /ram/OUT8
- IC4 pad 14: /word_conn2/IN9 -> /ram/OUT9
- IC4 pad 16: /word_conn2/IN10 -> /ram/OUT10
- IC4 pad 17: /word_conn2/IN11 -> /ram/OUT11
- IC4 pad 18: VCC -> +3.3V
- IC4 pad 19: /word_conn2/IN12 -> /ram/OUT12
- IC4 pad 2: /word_conn2/IN0 -> /ram/OUT0
- IC4 pad 20: /word_conn2/IN13 -> /ram/OUT13
- IC4 pad 22: /word_conn2/IN14 -> /ram/OUT14
- IC4 pad 23: /word_conn2/IN15 -> /ram/OUT15
- IC4 pad 24: /W0 -> /~{W1}
- IC4 pad 25: /E0 -> /E1
- IC4 pad 26: /ram/OUT15 -> /word_conn3/IN15
- IC4 pad 27: /ram/OUT14 -> /word_conn3/IN14
- IC4 pad 29: /ram/OUT13 -> /word_conn3/IN13
- IC4 pad 3: /word_conn2/IN1 -> /ram/OUT1
- IC4 pad 30: /ram/OUT12 -> /word_conn3/IN12
- IC4 pad 31: VCC -> +3.3V
- IC4 pad 32: /ram/OUT11 -> /word_conn3/IN11
- IC4 pad 33: /ram/OUT10 -> /word_conn3/IN10
- IC4 pad 35: /ram/OUT9 -> /word_conn3/IN9
- IC4 pad 36: /ram/OUT8 -> /word_conn3/IN8
- IC4 pad 37: /ram/OUT7 -> /word_conn3/IN7
- IC4 pad 38: /ram/OUT6 -> /word_conn3/IN6
- IC4 pad 40: /ram/OUT5 -> /word_conn3/IN5
- IC4 pad 41: /ram/OUT4 -> /word_conn3/IN4
- IC4 pad 42: VCC -> +3.3V
- IC4 pad 43: /ram/OUT3 -> /word_conn3/IN3
- IC4 pad 44: /ram/OUT2 -> /word_conn3/IN2
- IC4 pad 46: /ram/OUT1 -> /word_conn3/IN1
- IC4 pad 47: /ram/OUT0 -> /word_conn3/IN0
- IC4 pad 48: /E0 -> /E1
- IC4 pad 5: /word_conn2/IN2 -> /ram/OUT2
- IC4 pad 6: /word_conn2/IN3 -> /ram/OUT3
- IC4 pad 7: VCC -> +3.3V
- IC4 pad 8: /word_conn2/IN4 -> /ram/OUT4
- IC4 pad 9: /word_conn2/IN5 -> /ram/OUT5
- IC5 pad 1: /~{W1} -> GND
- IC5 pad 11: /ram/OUT6 -> /word_conn/IN6
- IC5 pad 12: /ram/OUT7 -> /word_conn/IN7
- IC5 pad 13: /ram/OUT8 -> /word_conn/IN8
- IC5 pad 14: /ram/OUT9 -> /word_conn/IN9
- IC5 pad 16: /ram/OUT10 -> /word_conn/IN10
- IC5 pad 17: /ram/OUT11 -> /word_conn/IN11
- IC5 pad 18: VCC -> +3.3V
- IC5 pad 19: /ram/OUT12 -> /word_conn/IN12
- IC5 pad 2: /ram/OUT0 -> /word_conn/IN0
- IC5 pad 20: /ram/OUT13 -> /word_conn/IN13
- IC5 pad 22: /ram/OUT14 -> /word_conn/IN14
- IC5 pad 23: /ram/OUT15 -> /word_conn/IN15
- IC5 pad 24: /~{W1} -> GND
- IC5 pad 25: /E1 -> /SEL
- IC5 pad 26: /word_conn3/IN15 -> /word_buffer/A15
- IC5 pad 27: /word_conn3/IN14 -> /ram/INA14
- IC5 pad 29: /word_conn3/IN13 -> /ram/INA13
- IC5 pad 3: /ram/OUT1 -> /word_conn/IN1
- IC5 pad 30: /word_conn3/IN12 -> /ram/INA12
- IC5 pad 31: VCC -> +3.3V
- IC5 pad 32: /word_conn3/IN11 -> /ram/INA11
- IC5 pad 33: /word_conn3/IN10 -> /ram/INA10
- IC5 pad 35: /word_conn3/IN9 -> /ram/INA9
- IC5 pad 36: /word_conn3/IN8 -> /ram/INA8
- IC5 pad 37: /word_conn3/IN7 -> /ram/INA7
- IC5 pad 38: /word_conn3/IN6 -> /ram/INA6
- IC5 pad 40: /word_conn3/IN5 -> /ram/INA5
- IC5 pad 41: /word_conn3/IN4 -> /ram/INA4
- IC5 pad 42: VCC -> +3.3V
- IC5 pad 43: /word_conn3/IN3 -> /ram/INA3
- IC5 pad 44: /word_conn3/IN2 -> /ram/INA2
- IC5 pad 46: /word_conn3/IN1 -> /ram/INA1
- IC5 pad 47: /word_conn3/IN0 -> /ram/INA0
- IC5 pad 48: /E1 -> /SEL
- IC5 pad 5: /ram/OUT2 -> /word_conn/IN2
- IC5 pad 6: /ram/OUT3 -> /word_conn/IN3
- IC5 pad 7: VCC -> +3.3V
- IC5 pad 8: /ram/OUT4 -> /word_conn/IN4
- IC5 pad 9: /ram/OUT5 -> /word_conn/IN5
- J1 pad 2: VCC -> GND
- J2 pad 1: /W1 -> /word_conn/IN0
- J2 pad 2: /W0 -> /word_conn/IN1
- J2 pad 3: /R1 -> /word_conn/IN2
- J2 pad 4: /R0 -> /word_conn/IN3
- J2 pad 5: /SEL -> /word_conn/IN4
- J3 pad 1: /word_conn/IN0 -> /word_conn1/IN0
- J3 pad 10: /word_conn/IN9 -> /word_conn1/IN9
- J3 pad 11: /word_conn/IN10 -> /word_conn1/IN10
- J3 pad 12: /word_conn/IN11 -> /word_conn1/IN11
- J3 pad 13: /word_conn/IN12 -> /word_conn1/IN12
- J3 pad 14: /word_conn/IN13 -> /word_conn1/IN13
- J3 pad 15: /word_conn/IN14 -> /word_conn1/IN14
- J3 pad 16: /word_conn/IN15 -> /word_conn1/IN15
- J3 pad 2: /word_conn/IN1 -> /word_conn1/IN1
- J3 pad 3: /word_conn/IN2 -> /word_conn1/IN2
- J3 pad 4: /word_conn/IN3 -> /word_conn1/IN3
- J3 pad 5: /word_conn/IN4 -> /word_conn1/IN4
- J3 pad 6: /word_conn/IN5 -> /word_conn1/IN5
- J3 pad 7: /word_conn/IN6 -> /word_conn1/IN6
- J3 pad 8: /word_conn/IN7 -> /word_conn1/IN7
- J3 pad 9: /word_conn/IN8 -> /word_conn1/IN8
- J4 pad 1: /word_conn1/IN0 -> /word_conn2/IN0
- J4 pad 10: /word_conn1/IN9 -> /word_conn2/IN9
- J4 pad 11: /word_conn1/IN10 -> /word_conn2/IN10
- J4 pad 12: /word_conn1/IN11 -> /word_conn2/IN11
- J4 pad 13: /word_conn1/IN12 -> /word_conn2/IN12
- J4 pad 14: /word_conn1/IN13 -> /word_conn2/IN13
- J4 pad 15: /word_conn1/IN14 -> /word_conn2/IN14
- J4 pad 16: /word_conn1/IN15 -> /word_conn2/IN15
- J4 pad 2: /word_conn1/IN1 -> /word_conn2/IN1
- J4 pad 3: /word_conn1/IN2 -> /word_conn2/IN2
- J4 pad 4: /word_conn1/IN3 -> /word_conn2/IN3
- J4 pad 5: /word_conn1/IN4 -> /word_conn2/IN4
- J4 pad 6: /word_conn1/IN5 -> /word_conn2/IN5
- J4 pad 7: /word_conn1/IN6 -> /word_conn2/IN6
- J4 pad 8: /word_conn1/IN7 -> /word_conn2/IN7
- J4 pad 9: /word_conn1/IN8 -> /word_conn2/IN8
- J5 pad 1: /word_conn2/IN0 -> /word_conn3/IN0
- J5 pad 10: /word_conn2/IN9 -> /word_conn3/IN9
- J5 pad 11: /word_conn2/IN10 -> /word_conn3/IN10
- J5 pad 12: /word_conn2/IN11 -> /word_conn3/IN11
- J5 pad 13: /word_conn2/IN12 -> /word_conn3/IN12
- J5 pad 14: /word_conn2/IN13 -> /word_conn3/IN13
- J5 pad 15: /word_conn2/IN14 -> /word_conn3/IN14
- J5 pad 16: /word_conn2/IN15 -> /word_conn3/IN15
- J5 pad 2: /word_conn2/IN1 -> /word_conn3/IN1
- J5 pad 3: /word_conn2/IN2 -> /word_conn3/IN2
- J5 pad 4: /word_conn2/IN3 -> /word_conn3/IN3
- J5 pad 5: /word_conn2/IN4 -> /word_conn3/IN4
- J5 pad 6: /word_conn2/IN5 -> /word_conn3/IN5
- J5 pad 7: /word_conn2/IN6 -> /word_conn3/IN6
- J5 pad 8: /word_conn2/IN7 -> /word_conn3/IN7
- J5 pad 9: /word_conn2/IN8 -> /word_conn3/IN8
- J6 pad 1: /word_conn3/IN0 -> /W1
- J6 pad 2: /word_conn3/IN1 -> /W0
- J6 pad 3: /word_conn3/IN2 -> /R1
- J6 pad 4: /word_conn3/IN3 -> /R0
- J6 pad 5: /word_conn3/IN4 -> /SEL
- J6 pad 6: /word_conn3/IN5 -> VCC
- J6 pad 7: /word_conn3/IN6 -> GND
- U1 pad 1: /SEL -> /R0
- U1 pad 2: /R0 -> /W0
- U1 pad 3: /R1 -> GND
- U1 pad 4: /R -> Net-(U1-Pad4)
- U1 pad 5: /W0 -> VCC
- U2 pad 1: Net-(U2-Pad1) -> /R1
- U2 pad 2: /~{SEL} -> /W1
- U2 pad 3: /E1 -> GND
- U2 pad 4: GND -> Net-(U2-Pad4)
- U2 pad 5: /SEL -> VCC
- U3 pad 1: /R -> Net-(U1-Pad4)
- U3 pad 2: /W -> /SEL
- U3 pad 4: Net-(U2-Pad1) -> /E0
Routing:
- net GND: track 0.00 -> 142.1 mm, vias 0 -> 60
- net /SEL: track 0.00 -> 89.8 mm, vias 0 -> 4
- net +3.3V: track 0.00 -> 65.5 mm, vias 0 -> 36
- net /~{SEL}: track 0.00 -> 58.8 mm, vias 0 -> 3
- net /W1: track 0.00 -> 51.3 mm, vias 0 -> 1
- net /W0: track 0.00 -> 45.8 mm, vias 0 -> 3
- net /W: track 0.00 -> 45.7 mm, vias 0 -> 2
- net VCC: track 0.00 -> 40.2 mm, vias 0 -> 6
- net /ram/OUT0: track 0.00 -> 39.1 mm
- net /ram/OUT1: track 0.00 -> 37.8 mm
- net /R: track 0.00 -> 37.6 mm, vias 0 -> 2
- net /ram/OUT2: track 0.00 -> 36.3 mm
- net /ram/OUT8: track 0.00 -> 35.1 mm, vias 0 -> 2
- net /ram/OUT3: track 0.00 -> 34.5 mm
- net /ram/OUT9: track 0.00 -> 34.0 mm, vias 0 -> 2
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- added copper zone on In2.Cu, net +3.3V
- added copper zone on F.Cu, net GND
- removed copper zone on F.Cu, net VCC
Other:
- board outline added: 47 x 72 mm
